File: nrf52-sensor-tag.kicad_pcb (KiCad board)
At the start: 2 copper layers, 36 x 36 mm, 20 parts, among them IC2 VEML6030, IC3 MS860702BA01-50, J3 Conn_01x07_Male, U1 MS88SF2

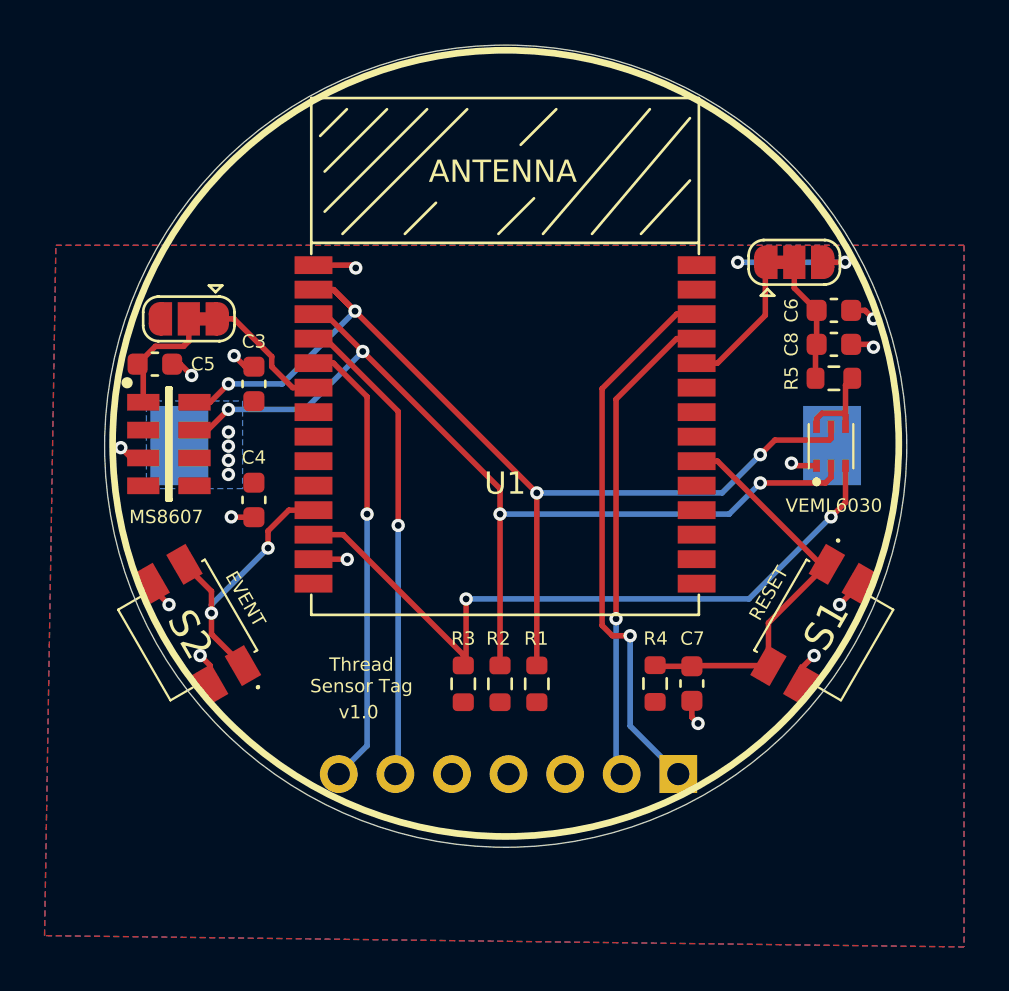
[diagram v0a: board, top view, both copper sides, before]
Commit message: Removed unneseccary components because the battery is a very undisturbed source
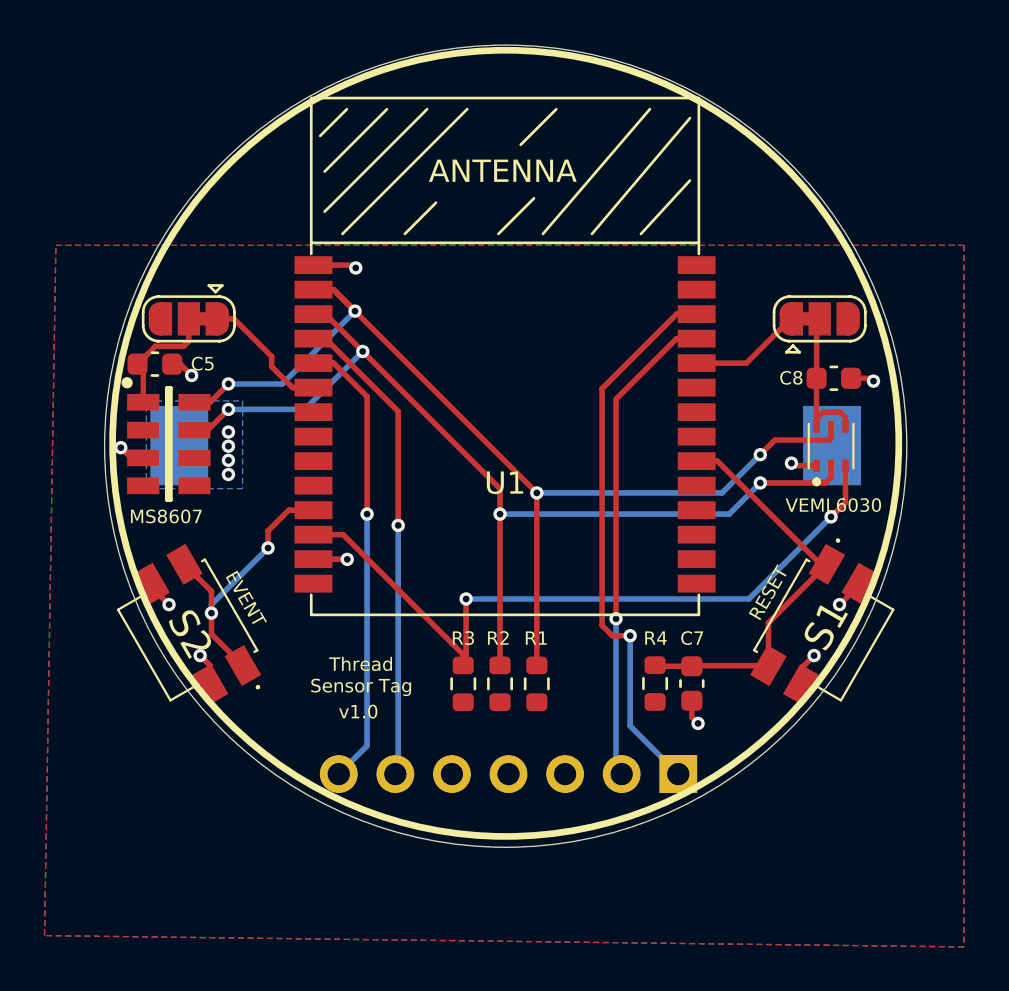
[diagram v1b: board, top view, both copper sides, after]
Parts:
- removed C3, C6: 10uF, Capacitor_SMD:C_0603_1608Metric
- removed C4: 0.1uF, Capacitor_SMD:C_0603_1608Metric
- removed R5: 10R, Resistor_SMD:R_0603_1608Metric
- moved JP2 2.79 mm to (135.9, 58.9)
- moved C8 1.52 mm to (136.5, 61.6)
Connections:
- C8 pad 1: Net-(C6-Pad1) -> Net-(C8-Pad1)
- IC2 pad 4: Net-(IC2-Pad4) -> Net-(C8-Pad1)
- IC2 pad 6: Net-(IC2-Pad4) -> Net-(C8-Pad1)
- JP2 pad 2: Net-(C6-Pad1) -> Net-(C8-Pad1)
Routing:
- net Net-(C8-Pad1): track 0.00 -> 7.21 mm
- net /VCC: track 5.81 -> 0.00 mm, vias 6 -> 4
- net Net-(C6-Pad1): track 5.64 -> 0.00 mm
- net Net-(IC2-Pad4): track 4.61 -> 0.00 mm
- net GND: track 18.4 -> 15.2 mm, vias 14 -> 11
- net /SENS2_VCC: track 6.15 -> 4.85 mm

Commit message: Add RGB LED
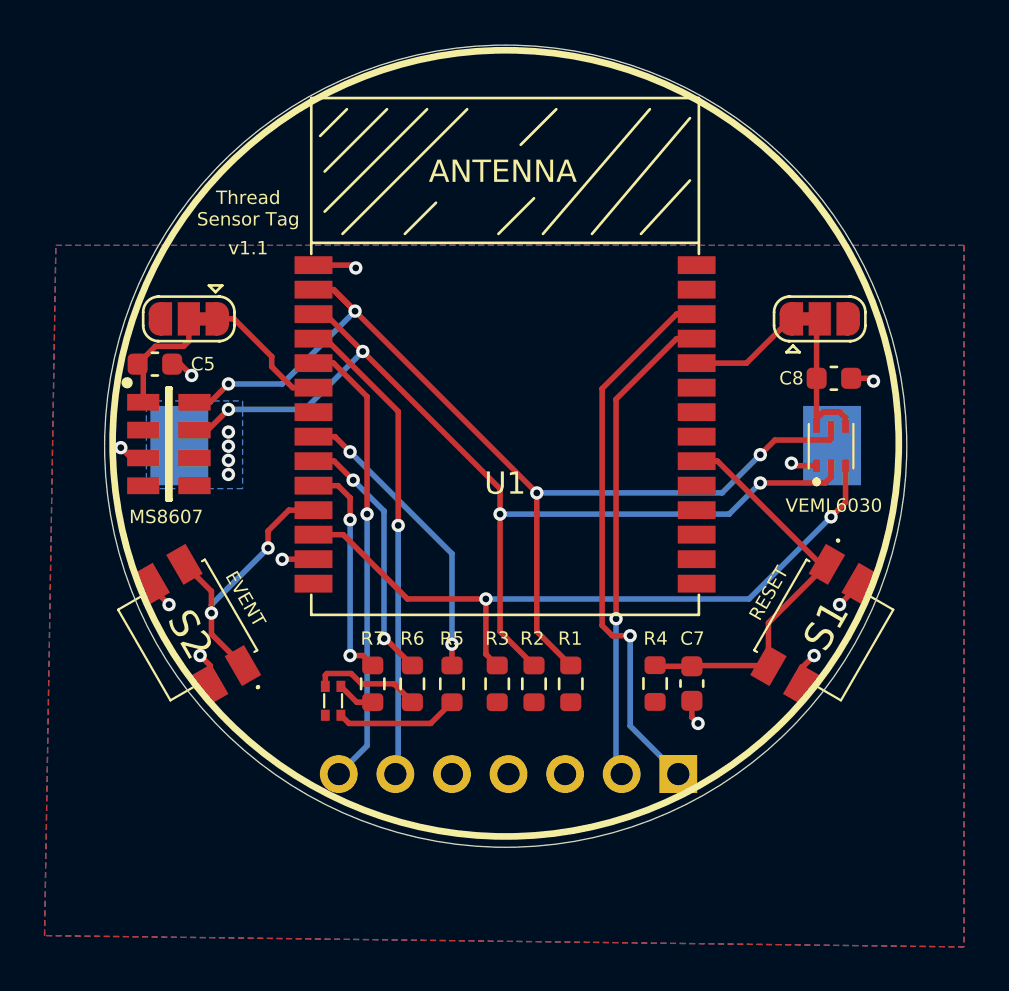
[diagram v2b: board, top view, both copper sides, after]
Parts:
- added LED1: APHF1608LSEEQBDZGKC, APHF1608LSEEQBDZGKC:APHF1608LSEEQBDZGKC, F.Cu at (114.0, 76.1)
- added R5: 1k2, Resistor_SMD:R_0603_1608Metric, F.Cu at (119.4, 75.3)
- added R6: 2k2, Resistor_SMD:R_0603_1608Metric, F.Cu at (117.6, 75.3)
- added R7: 390R, Resistor_SMD:R_0603_1608Metric, F.Cu at (115.8, 75.3)
- moved R1 1.52 mm to (124.7, 75.3)
- moved R2 1.52 mm to (123.0, 75.3)
- moved R3 1.52 mm to (121.4, 75.3)
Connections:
- U1 pad 10: Net-(U1-Pad10) -> /LED_BLUE
- U1 pad 8: Net-(U1-Pad8) -> /LED_RED
- U1 pad 9: Net-(U1-Pad9) -> /LED_GREEN
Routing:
- net /LED_RED: track 0.00 -> 13.4 mm, vias 0 -> 2
- net /LED_GREEN: track 0.00 -> 11.6 mm, vias 0 -> 2
- net /LED_BLUE: track 0.00 -> 10.2 mm, vias 0 -> 2
- net Net-(LED1-Pad2): track 0.00 -> 5.53 mm
- net Net-(LED1-Pad4): track 0.00 -> 4.97 mm
- net Net-(LED1-Pad3): track 0.00 -> 1.72 mm
- net /INT1: track 33.2 -> 31.9 mm
- net /SDA: track 44.8 -> 45.5 mm
- net /SCL: track 46.8 -> 47.4 mm
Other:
- board text added: "v1.1"
- board text removed: "v1.0"
